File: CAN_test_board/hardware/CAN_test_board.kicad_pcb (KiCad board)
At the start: 2 copper layers, 18 x 18.5 mm, 12 parts, among them IC1 TJA1050T, J3 Conn_01x06, U4 level shifter

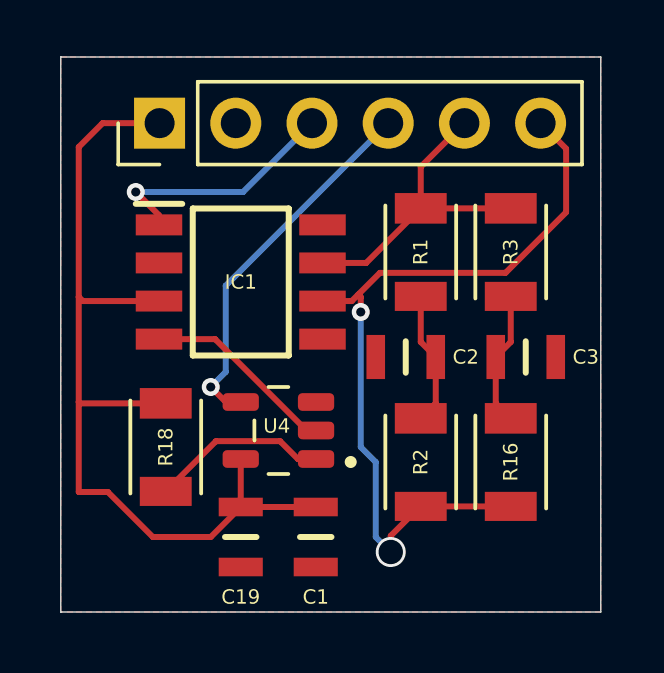
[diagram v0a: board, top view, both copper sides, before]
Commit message: fixed can test circuit via sizing
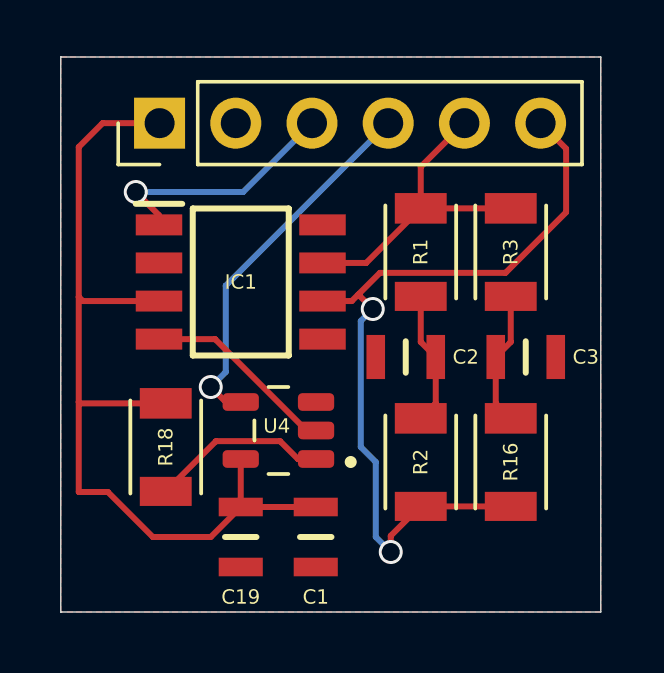
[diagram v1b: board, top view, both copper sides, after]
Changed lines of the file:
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@@
 	(via
 		(at 152.5 86.5)
-		(size 0.6)
-		(drill 0.3)
+		(size 0.8)
+		(drill 0.6)
 		(layers "F.Cu" "B.Cu")
 		(net "/CAN TX")
@@
 	(via
 		(at 155 93)
-		(size 0.6)
-		(drill 0.3)
+		(size 0.8)
+		(drill 0.6)
 		(layers "F.Cu" "B.Cu")
 		(net "/CAN RX_1")
@@
 	)
 	(segment
+		(start 160.4 90.4)
+		(end 159.9175 89.9175)
+		(width 0.2)
+		(layer "F.Cu")
+		(net "/CANL")
+	)
+	(segment
 		(start 165 96.98)
 		(end 162 96.98)
@@
 	)
 	(segment
-		(start 160 90)
-		(end 160 90.5)
-		(width 0.2)
-		(layer "F.Cu")
-		(net "/CANL")
-	)
-	(segment
-		(start 159.9175 89.9175)
-		(end 160 90)
-		(width 0.2)
-		(layer "F.Cu")
-		(net "/CANL")
-	)
-	(segment
 		(start 161.98 96.98)
 		(end 162 96.98)
@@
 	)
 	(via
-		(at 160 90.5)
-		(size 0.6)
-		(drill 0.3)
+		(at 160.4 90.4)
+		(size 0.8)
+		(drill 0.6)
 		(layers "F.Cu" "B.Cu")
 		(net "/CANL")
@@
 	(via
 		(at 161 98.5)
-		(size 1)
-		(drill 0.813)
-		(layers "F.Cu" "B.Cu")
+		(size 0.8)
+		(drill 0.6)
+		(layers "F.Cu" "B.Cu")
+		(net "/CANL")
+	)
+	(segment
+		(start 160.4 90.4)
+		(end 160 90.8)
+		(width 0.2)
+		(layer "B.Cu")
+		(net "/CANL")
+	)
+	(segment
+		(start 160.5 95.5)
+		(end 160.5 98)
+		(width 0.2)
+		(layer "B.Cu")
+		(net "/CANL")
+	)
+	(segment
+		(start 160 95)
+		(end 160.5 95.5)
+		(width 0.2)
+		(layer "B.Cu")
 		(net "/CANL")
 	)
 	(segment
 		(start 160.5 98)
-		(end 160.5 95.5)
-		(width 0.2)
-		(layer "B.Cu")
-		(net "/CANL")
-	)
-	(segment
-		(start 161 98.5)
-		(end 160.5 98)
-		(width 0.2)
-		(layer "B.Cu")
-		(net "/CANL")
-	)
-	(segment
-		(start 160.5 95.5)
+		(end 161 98.5)
+		(width 0.2)
+		(layer "B.Cu")
+		(net "/CANL")
+	)
+	(segment
+		(start 160 90.8)
 		(end 160 95)
 		(width 0.2)
 		(layer "B.Cu")
-		(net "/CANL")
-	)
-	(segment
-		(start 160 95)
-		(end 160 90.5)
-		(width 0.2)
-		(layer "B.Cu")

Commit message: fixed can test circuit via sizing
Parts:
- moved R1 1.00 mm to (163.0, 88.5)
- moved R18 0.90 mm to (152.6, 95.0)
- moved R3 0.80 mm to (165.8, 88.5)
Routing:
- net /CANL: track 27.4 -> 29.5 mm
- net /CANH: track 10.5 -> 11.7 mm
- net /CAN RX_1: track 12.5 -> 13.5 mm
- net Net-(U4-~{OE}): track 5.95 -> 6.85 mm
- net /5V: track 30.7 -> 30.0 mm

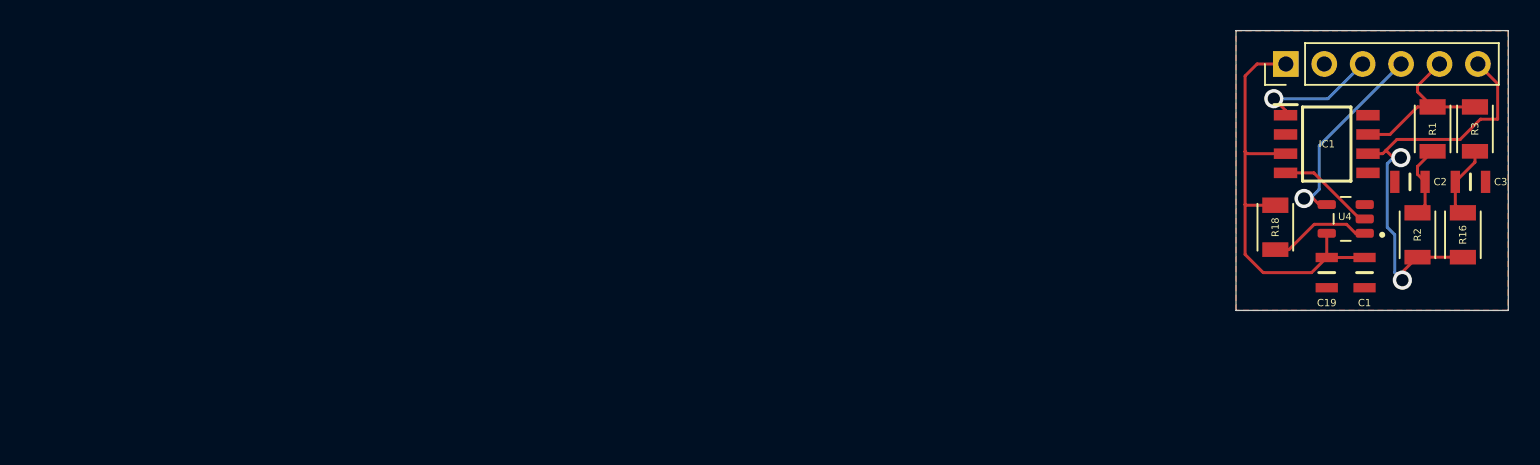
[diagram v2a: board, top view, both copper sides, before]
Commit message: fixes to can circuitry
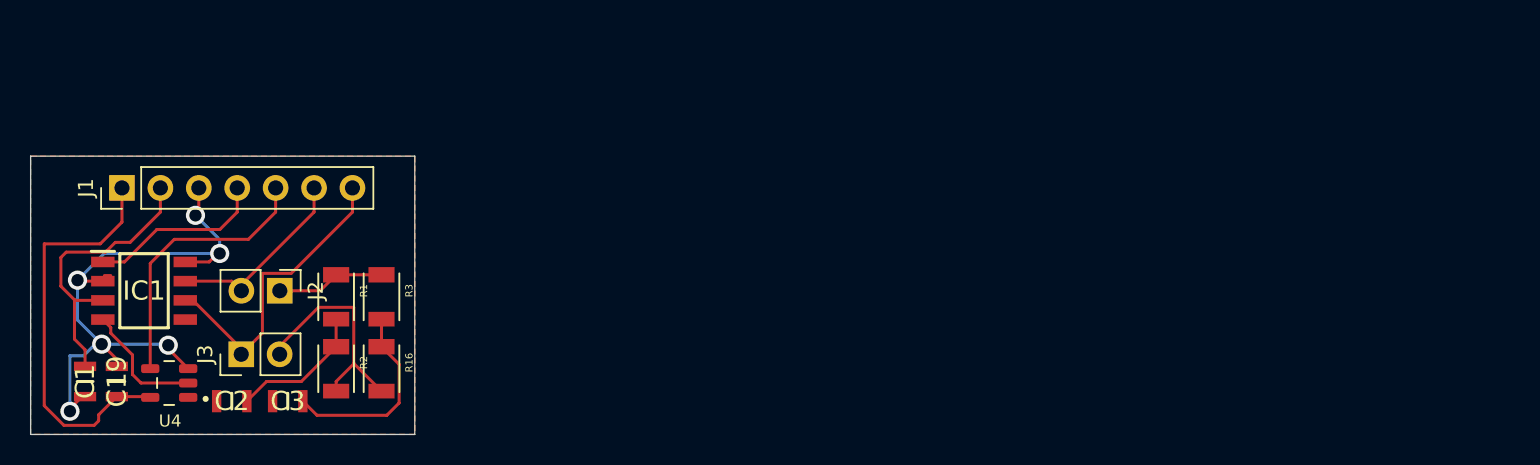
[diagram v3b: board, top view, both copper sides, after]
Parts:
- removed R18: 1k, CAN_test_board:RESC3116X65N
- added J1: Conn_01x07, Connector_PinHeader_2.54mm:PinHeader_1x07_P2.54mm_Vertical, F.Cu at (76.3, 92.4)
- added J2: Conn_01x02, Connector_PinHeader_2.54mm:PinHeader_1x02_P2.54mm_Vertical, F.Cu at (86.8, 99.2)
- J3: value Conn_01x06 -> Conn_01x02; footprint Connector_PinHeader_2.54mm:PinHeader_1x06_P2.54mm_Vertical -> Connector_PinHeader_2.54mm:PinHeader_1x02_P2.54mm_Vertical
- moved C1 84.9 mm to (73.9, 105.2)
- moved C19 80.3 mm to (76.0, 105.2), turned to -90 degrees
- moved C3 79.5 mm to (87.3, 106.5), turned to 0 degrees
- moved C2 79.2 mm to (83.6, 106.5)
- moved IC1 78.8 mm to (77.8, 99.2)
- moved U4 78.5 mm to (79.5, 105.3)
- moved R1 73.3 mm to (90.5, 99.6)
- moved R3 73.1 mm to (93.5, 99.6)
- moved R16 72.0 mm to (93.5, 104.4)
- moved R2 72.0 mm to (90.5, 104.4)
- moved J3 71.7 mm to (84.2, 103.4)
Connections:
- C19 pad 2: /5V -> /3V3
- J3 pad 1: /5V -> /CANL
- J3 pad 2: GND -> Net-(J3-Pin_2)
- R1 pad 1: /CANH -> Net-(J2-Pin_1)
- R16 pad 2: /CANL -> Net-(J3-Pin_2)
- R2 pad 2: /CANL -> Net-(J3-Pin_2)
- R3 pad 1: /CANH -> Net-(J2-Pin_1)
- U4 pad 1: Net-(U4-~{OE}) -> GND
- U4 pad 5: /5V -> /3V3
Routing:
- net GND: track 0.75 -> 40.9 mm, vias 0 -> 6
- net /3V3: track 0.00 -> 27.3 mm
- net Net-(J3-Pin_2): track 0.00 -> 15.1 mm
- net /5V: track 30.0 -> 19.2 mm
- net /CANL: track 29.5 -> 20.6 mm, vias 2 -> 0
- net Net-(C3-Pad2): track 4.81 -> 13.1 mm
- net Net-(J2-Pin_1): track 0.00 -> 7.16 mm
- net Net-(U4-~{OE}): track 6.85 -> 0.00 mm
- net /CAN RX_1: track 13.5 -> 18.3 mm, vias 1 -> 0
- net Net-(C2-Pad2): track 4.89 -> 9.21 mm
- net /CAN TX: track 8.24 -> 11.9 mm, vias 1 -> 0
- net /CAN RX: track 6.50 -> 8.35 mm
- net /CANH: track 11.7 -> 12.8 mm
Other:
- board size 18 x 18.5 mm -> 25.4 x 18.4 mm
